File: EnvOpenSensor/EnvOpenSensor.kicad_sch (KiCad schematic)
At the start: 31 parts, among them J1 USB_C_Receptacle_USB2.0_16P, J2 AVR-ISP-6, SW1 SW_Push, SW2 SW_Push, SW3 SW_Push, SW4 SW_Push, U1 SCD41-D-R2, U2 Si7021-A20, U3 SPX3819M5-L-3-3, U4 ATtiny85-20S

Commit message: commit current version
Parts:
- added C0, C10, C11, C5: 0402 0.1uF, Capacitor_SMD:C_0402_1005Metric, symbol Device:C_Small
- added C12, C13, C6, C7: 0402 1uF, Capacitor_SMD:C_0402_1005Metric, symbol Device:C_Small
- added C14, C15, C8, C9: 0402 10uF, Capacitor_SMD:C_0402_1005Metric, symbol Device:C_Small
- added IC1, IC2, IC3, IC4: IS31FL3730-QFLS2-TR, Package_DFN_QFN:QFN-24-1EP_4x4mm_P0.5mm_EP2.6x2.6mm_ThermalVias, symbol IS31FL3730-QFLS2-TR:IS31FL3730-QFLS2-TR
- added NT0: NetTie_2, NetTie:NetTie-2_SMD_Pad0.5mm, symbol Device:NetTie_2
- H1, H2, H3, H4: value MountingHole -> DIY-305-ountingHole
- U3: value SPX3819M5-L-3-3 -> SPX3819DIY-305-5-L-3-3
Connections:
- net +3V3: now also IC1.3 (SDB), IC1.6 (AD), IC2.3 (SDB), IC3.3 (SDB), IC4.3 (SDB)
- net GND: now also C0.2, C10.2, C11.2, C12.2, C13.2, C14.2, C15.2, C5.2, C6.2, C7.2, C8.2, C9.2, IC1.20 (GND_1), IC1.25 (GND_2), IC2.20 (GND_1), IC2.25 (GND_2), IC3.20 (GND_1), IC3.25 (GND_2), IC4.20 (GND_1), IC4.25 (GND_2), IC4.6 (AD)
- net PB0: now also IC1.1 (SDA), IC2.1 (SDA), IC2.6 (AD), IC3.1 (SDA), IC4.1 (SDA)
- net PB2: now also IC1.2 (SCL), IC2.2 (SCL), IC3.2 (SCL), IC3.6 (AD), IC4.2 (SCL)
- net VBUS: now also NT0.1
- net IC2C2: now reaches DIY-305-0.1 (Col2)
- net IC2C2: now also DIY-305-1.12 (Row2), IC4.23 (C2)
- net IC2R6: now reaches DIY-305-0.10 (Row6)
- net IC2R6: now also IC4.13 (R6/C11)
- net IC2R5: now reaches DIY-305-0.11 (Row5)
- net IC2R5: now also DIY-305-1.13 (Col5), IC4.12 (R5)
- net IC2R2: now reaches DIY-305-0.12 (Row2)
- net IC2R2: now also DIY-305-1.1 (Col2), IC4.8 (R2)
- net IC2C5: now reaches DIY-305-0.13 (Col5)
- net IC2C5: now also DIY-305-1.11 (Row5), IC4.19 (C5)
- net IC2C4: now reaches DIY-305-0.14 (Col4)
- net IC2C4: now also DIY-305-1.4 (Row4), IC4.21 (C4)
- net IC2R1: now reaches DIY-305-0.2 (Row1)
- net IC2R1: now also DIY-305-1.5 (Col1), IC4.7 (R1)
- net IC2R3: now reaches DIY-305-0.3 (Row3)
- net IC2R3: now also DIY-305-1.8 (Col3), IC4.9 (R3)
- net IC2R4: now reaches DIY-305-0.4 (Row4)
- net IC2R4: now also DIY-305-1.14 (Col4), IC4.10 (R4)
- net IC2C1: now reaches DIY-305-0.5 (Col1)
- net IC2C1: now also DIY-305-1.2 (Row1), IC4.24 (C1)
- net IC2C8: now reaches DIY-305-0.7 (Dot)
- net IC2C8: now also IC4.16 (C8)
- net IC2C3: now reaches DIY-305-0.8 (Col3)
- net IC2C3: now also DIY-305-1.3 (Row3), IC4.22 (C3)
- net IC2R7: now reaches DIY-305-0.9 (Row7)
- net IC2R7: now also IC4.14 (R7/C10)
- net IC4R2: now reaches DIY-305-7.1 (Col2)
- net IC4R2: now also DIY-305-6.12 (Row2), IC3.8 (R2)
- net IC4C6: now reaches DIY-305-7.10 (Row6)
- net IC4C6: now also IC3.18 (C6)
- net IC4C5: now reaches DIY-305-7.11 (Row5)
- net IC4C5: now also DIY-305-6.13 (Col5), IC3.19 (C5)
- net IC4C2: now reaches DIY-305-7.12 (Row2)
- net IC4C2: now also DIY-305-6.1 (Col2), IC3.23 (C2)
- net IC4R5: now reaches DIY-305-7.13 (Col5)
- net IC4R5: now also DIY-305-6.11 (Row5), IC3.12 (R5)
- net IC4R4: now reaches DIY-305-7.14 (Col4)
- net IC4R4: now also DIY-305-6.4 (Row4), IC3.10 (R4)
- net IC4C1: now reaches DIY-305-7.2 (Row1)
- net IC4C1: now also DIY-305-6.5 (Col1), IC3.24 (C1)
- net IC4C3: now reaches DIY-305-7.3 (Row3)
- net IC4C3: now also DIY-305-6.8 (Col3), IC3.22 (C3)
- net IC4C4: now reaches DIY-305-7.4 (Row4)
- net IC4C4: now also DIY-305-6.14 (Col4), IC3.21 (C4)
- net IC4R1: now reaches DIY-305-7.5 (Col1)
- net IC4R1: now also DIY-305-6.2 (Row1), IC3.7 (R1)
- net IC4R8: now reaches DIY-305-7.7 (Dot)
- net IC4R8: now also IC3.15 (R8/C9)
- net IC4R3: now reaches DIY-305-7.8 (Col3)
- net IC4R3: now also DIY-305-6.3 (Row3), IC3.9 (R3)
- net IC4C7: now reaches DIY-305-7.9 (Row7)
- net IC4C7: now also IC3.17 (C7)
- net IC2C6: now reaches DIY-305-1.10 (Row6)
- net IC2C6: now also IC4.18 (C6)
- net IC2R8: now reaches DIY-305-1.7 (Dot)
- net IC2R8: now also IC4.15 (R8/C9)
- net IC2C7: now reaches DIY-305-1.9 (Row7)
- net IC2C7: now also IC4.17 (C7)
- net IC3R2: now reaches DIY-305-5.1 (Col2)
- net IC3R2: now also DIY-305-4.12 (Row2), IC2.8 (R2)
- net IC3C6: now reaches DIY-305-5.10 (Row6)
- net IC3C6: now also IC2.18 (C6)
- net IC3C5: now reaches DIY-305-5.11 (Row5)
- net IC3C5: now also DIY-305-4.13 (Col5), IC2.19 (C5)
- net IC3C2: now reaches DIY-305-5.12 (Row2)
- net IC3C2: now also DIY-305-4.1 (Col2), IC2.23 (C2)
- net IC3R5: now reaches DIY-305-5.13 (Col5)
- net IC3R5: now also DIY-305-4.11 (Row5), IC2.12 (R5)
- net IC3R4: now reaches DIY-305-5.14 (Col4)
- net IC3R4: now also DIY-305-4.4 (Row4), IC2.10 (R4)
- net IC3C1: now reaches DIY-305-5.2 (Row1)
- net IC3C1: now also DIY-305-4.5 (Col1), IC2.24 (C1)
- net IC3C3: now reaches DIY-305-5.3 (Row3)
- net IC3C3: now also DIY-305-4.8 (Col3), IC2.22 (C3)
- net IC3C4: now reaches DIY-305-5.4 (Row4)
- net IC3C4: now also DIY-305-4.14 (Col4), IC2.21 (C4)
- net IC3R1: now reaches DIY-305-5.5 (Col1)
- net IC3R1: now also DIY-305-4.2 (Row1), IC2.7 (R1)
- net IC3R8: now reaches DIY-305-5.7 (Dot)
- net IC3R8: now also IC2.15 (R8/C9)
- net IC3R3: now reaches DIY-305-5.8 (Col3)
- net IC3R3: now also DIY-305-4.3 (Row3), IC2.9 (R3)
- net IC3C7: now reaches DIY-305-5.9 (Row7)
- net IC3C7: now also IC2.17 (C7)
- net IC1R2: now reaches DIY-305-3.1 (Col2)
- net IC1R2: now also DIY-305-2.12 (Row2), IC1.8 (R2)
- net IC1C6: now reaches DIY-305-3.10 (Row6)
- net IC1C6: now also IC1.18 (C6)
- net IC1C5: now reaches DIY-305-3.11 (Row5)
- net IC1C5: now also DIY-305-2.13 (Col5), IC1.19 (C5)
- net IC1C2: now reaches DIY-305-3.12 (Row2)
- net IC1C2: now also DIY-305-2.1 (Col2), IC1.23 (C2)
- net IC1R5: now reaches DIY-305-3.13 (Col5)
- net IC1R5: now also DIY-305-2.11 (Row5), IC1.12 (R5)
- net IC1R4: now reaches DIY-305-3.14 (Col4)
- net IC1R4: now also DIY-305-2.4 (Row4), IC1.10 (R4)
- net IC1C1: now reaches DIY-305-3.2 (Row1)
- net IC1C1: now also DIY-305-2.5 (Col1), IC1.24 (C1)
- net IC1C3: now reaches DIY-305-3.3 (Row3)
- net IC1C3: now also DIY-305-2.8 (Col3), IC1.22 (C3)
- net IC1C4: now reaches DIY-305-3.4 (Row4)
- net IC1C4: now also DIY-305-2.14 (Col4), IC1.21 (C4)
- net IC1R1: now reaches DIY-305-3.5 (Col1)
- net IC1R1: now also DIY-305-2.2 (Row1), IC1.7 (R1)
- net IC1R8: now reaches DIY-305-3.7 (Dot)
- net IC1R8: now also IC1.15 (R8/C9)
- net IC1R3: now reaches DIY-305-3.8 (Col3)
- net IC1R3: now also DIY-305-2.3 (Row3), IC1.9 (R3)
- net IC1C7: now reaches DIY-305-3.9 (Row7)
- net IC1C7: now also IC1.17 (C7)
- net IC3R6: now reaches DIY-305-4.10 (Row6)
- net IC3R6: now also IC2.13 (R6/C11)
- net IC3C8: now reaches DIY-305-4.7 (Dot)
- net IC3C8: now also IC2.16 (C8)
- net IC3R7: now reaches DIY-305-4.9 (Row7)
- net IC3R7: now also IC2.14 (R7/C10)
- net IC1R6: now reaches DIY-305-2.10 (Row6)
- net IC1R6: now also IC1.13 (R6/C11)
- net IC1C8: now reaches DIY-305-2.7 (Dot)
- net IC1C8: now also IC1.16 (C8)
- net IC1R7: now reaches DIY-305-2.9 (Row7)
- net IC1R7: now also IC1.14 (R7/C10)
- net IC4R6: now reaches DIY-305-6.10 (Row6)
- net IC4R6: now also IC3.13 (R6/C11)
- net IC4C8: now reaches DIY-305-6.7 (Dot)
- net IC4C8: now also IC3.16 (C8)
- net IC4R7: now reaches DIY-305-6.9 (Row7)
- net IC4R7: now also IC3.14 (R7/C10)
- new net VCC: C0.1, C10.1, C11.1, C12.1, C13.1, C14.1, C15.1, C5.1, C6.1, C7.1, C8.1, C9.1, IC1.11 (VCC), IC2.11 (VCC), IC3.11 (VCC), IC4.11 (VCC), NT0.2

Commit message: let autorouter go crazy
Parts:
- added C16: 0402 0.1uF, Capacitor_SMD:C_0402_1005Metric, symbol Device:C_Small
- added C17: 0402 1uF, Capacitor_SMD:C_0402_1005Metric, symbol Device:C_Small
- added C18: 0402 10uF, Capacitor_SMD:C_0402_1005Metric, symbol Device:C_Small
- added R0, R10, R11, R12, R13, R14, R15, R16, R6, R7, R8, R9: 10K 0402, Resistor_SMD:R_0402_1005Metric, symbol Device:R_Small
- added U0: TCA9548ARGER, Package_DFN_QFN:Texas_RGE0024C_EP2.1x2.1mm, symbol Interface_Expansion:TCA9548ARGER
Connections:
- net +3V3: now also C16.1, C17.1, C18.1, R0.2, R10.2, R11.2, R12.2, R13.2, R14.2, R15.2, R16.2, R6.2, R7.2, R8.2, R9.2, U0.21 (VCC)
- net GND: now also C16.2, C17.2, C18.2, U0.18 (A2), U0.22 (A0), U0.23 (A1), U0.9 (GND)
- net PB0: now also U0.20 (SDA); no longer IC1.1 (SDA), IC2.1 (SDA), IC2.6 (AD), IC3.1 (SDA), IC4.1 (SDA), U1.10 (SDA), U2.1 (SDA)
- net PB2: now also U0.19 (SCL); no longer IC1.2 (SCL), IC2.2 (SCL), IC3.2 (SCL), IC3.6 (AD), IC4.2 (SCL), U1.9 (SCL), U2.6 (SCL)
- new net SCL0_3V3: R16.1, U0.2 (SC0), U2.6 (SCL)
- new net SCL1_3V3: R14.1, U0.4 (SC1), U1.9 (SCL)
- new net SCL2_3V3: IC1.2 (SCL), R7.1, U0.6 (SC2)
- new net SCL3_3V3: IC2.2 (SCL), R0.1, U0.8 (SC3)
- new net SCL4_3V3: IC3.2 (SCL), IC3.6 (AD), R9.1, U0.11 (SC4)
- new net SCL5_3V3: IC4.2 (SCL), R11.1, U0.13 (SC5)
- new net SCL6_3V3: U0.15 (SC6)
- new net SCL7_3V3: U0.17 (SC7)
- new net SDA0_3V3: R15.1, U0.1 (SD0), U2.1 (SDA)
- new net SDA1_3V3: R13.1, U0.3 (SD1), U1.10 (SDA)
- new net SDA2_3V3: IC1.1 (SDA), R8.1, U0.5 (SD2)
- new net SDA3_3V3: IC2.1 (SDA), IC2.6 (AD), R6.1, U0.7 (SD3)
- new net SDA4_3V3: IC3.1 (SDA), R10.1, U0.10 (SD4)
- new net SDA5_3V3: IC4.1 (SDA), R12.1, U0.12 (SD5)
- new net SDA6_3V3: U0.14 (SD6)
- new net SDA7_3V3: U0.16 (SD7)

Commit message: generated production files
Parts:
- J1: value USB_C_Receptacle_USB2.0_16P -> HRO_TYPE-C-31-M-12
- U3: value SPX3819DIY-305-5-L-3-3 -> LDO SOT-23-5 3.3V
- renumbered C1 to C_BYP_1
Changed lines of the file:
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@@
   (symbol (lib_id "Device:C_Small") (at 100.33 29.21 0) (unit 1)
     (in_bom yes) (on_board yes) (dnp no)
-    (property "Reference" "C1" (at 100.965 27.94 0)
+    (property "Reference" "C_BYP_1" (at 101.6 27.94 0)
       (effects (font (size 0.25 0.25)))
     )
@@
       (project "EnvOpenSensor"
         (path "/2bbc1dac-4f9d-46a0-a466-6585abe7fd58"
-          (reference "C1") (unit 1)
+          (reference "C_BYP_1") (unit 1)
         )
       )
@@
       (effects (font (size 1.27 1.27)))
     )
-    (property "Value" "SPX3819DIY-305-5-L-3-3" (at 92.075 17.78 0)
+    (property "Value" "LDO SOT-23-5 3.3V" (at 92.075 17.78 0)
       (effects (font (size 1.27 1.27)))
     )
@@
       (effects (font (size 1.27 1.27)))
     )
-    (property "Value" "USB_C_Receptacle_USB2.0_16P" (at 31.115 20.32 0)
-      (effects (font (size 1.27 1.27)))
-    )
+    (property "Value" "HRO_TYPE-C-31-M-12" (at 31.115 20.32 0)
+      (effects (font (size 1.27 1.27)))
+    )

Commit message: began re-work on fixing colossal mistakes
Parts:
- removed C10, C11, C5: 0402 0.1uF, Capacitor_SMD:C_0402_1005Metric, symbol Device:C_Small
- removed C12, C13, C7: 0402 1uF, Capacitor_SMD:C_0402_1005Metric, symbol Device:C_Small
- removed C14, C15, C9: 0402 10uF, Capacitor_SMD:C_0402_1005Metric, symbol Device:C_Small
- added C104, C107, C110: 0402 0.1uF, Capacitor_SMD:C_0402_1005Metric, symbol Device:C_Small
- added C105, C108, C111: 0402 1uF, Capacitor_SMD:C_0402_1005Metric, symbol Device:C_Small
- added C106, C109, C112: 0402 10uF, Capacitor_SMD:C_0402_1005Metric, symbol Device:C_Small
- renumbered C0 to C101, C6 to C102, C8 to C103, DIY-305-2 to DIY-305-1, DIY-305-3 to DIY-305-2, DIY-305-0 to DIY-305-3, DIY-305-1 to DIY-305-4, DIY-305-4 to DIY-305-5, DIY-305-5 to DIY-305-6, DIY-305-6 to DIY-305-7, DIY-305-7 to DIY-305-8, IC4 to IC2, IC2 to IC3, IC3 to IC4, R7 to R101, R8 to R102, R11 to R103, R12 to R104, R0 to R105, R6 to R106, R9 to R107, R10 to R108
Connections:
- net GND: now also C104.2, C105.2, C106.2, C107.2, C108.2, C109.2, C110.2, C111.2, C112.2
- net SCL2_3V3: no longer IC1.2 (SCL), R101.1
- net SCL3_3V3: no longer IC3.2 (SCL), R105.1
- net SCL5_3V3: now also IC3.2 (SCL), R105.1; no longer IC2.2 (SCL), R103.1
- net SCL6_3V3: now also IC2.2 (SCL), R103.1
- net SCL7_3V3: now also IC1.2 (SCL), R101.1
- net SDA2_3V3: no longer IC1.1 (SDA), R102.1
- net SDA3_3V3: no longer IC3.1 (SDA), IC3.6 (AD), R106.1
- net SDA5_3V3: now also IC3.1 (SDA), IC3.6 (AD), R106.1; no longer IC2.1 (SDA), R104.1
- net SDA6_3V3: now also IC2.1 (SDA), R104.1
- net SDA7_3V3: now also IC1.1 (SDA), R102.1
- net VCC: now also C104.1, C105.1, C106.1, C107.1, C108.1, C109.1, C110.1, C111.1, C112.1
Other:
- moved on the sheet: C101, C102, C103, DIY-305-1, DIY-305-2, DIY-305-3, DIY-305-4, DIY-305-5, DIY-305-6, DIY-305-7, DIY-305-8, IC1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

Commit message: swapped LDO for more capable switching regulator
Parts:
- removed C2, C3, C_BYP_1: 10nF 0402, Capacitor_SMD:C_0402_1005Metric, symbol Device:C_Small
- removed R3: 10K 0402, Resistor_SMD:R_0402_1005Metric, symbol Device:R_Small
- removed U3: LDO SOT-23-5 3.3V, Package_TO_SOT_SMD:SOT-23-5, symbol Regulator_Linear:SPX3819M5-L-3-3
- added C1, C6, C7: 10uF 0402, Capacitor_SMD:C_0402_1005Metric, symbol Device:C_Small
- added C5: 0.1uF 0402, Capacitor_SMD:C_0402_1005Metric, symbol Device:C_Small
- added L1: SPH3015H2R2MT, Inductor_SMD:L_Sunlord_SWPA3015S, symbol Device:L_Small
- added R6: 100ohm 0402, Resistor_SMD:R_0402_1005Metric, symbol Device:R_Small
- added U5: TPS63001DRCR, Package_SON:Texas_DRC0010J_ThermalVias, symbol Regulator_Switching:TPS63001
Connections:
- net +3V3: now also NT0.1, C6.1, C7.1, U5.1 (VOUT), U5.10 (FB)
- net GND: now also C1.2, C5.2, C6.2, C7.2, U5.11 (PGND), U5.3 (PGND), U5.9 (GND)
- net VBUS: now also C1.1, R6.1, U5.5 (VIN); no longer NT0.1
- new net: C5.1, R6.2, U5.6 (EN), U5.7 (PS/SYNC), U5.8 (VINA)
- new net: L1.2, U5.2 (L2)
- new net: L1.1, U5.4 (L1)
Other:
- moved on the sheet: C101, C102, C103, C104, C105, C106, C107, C108, C109, C110, C111, C112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

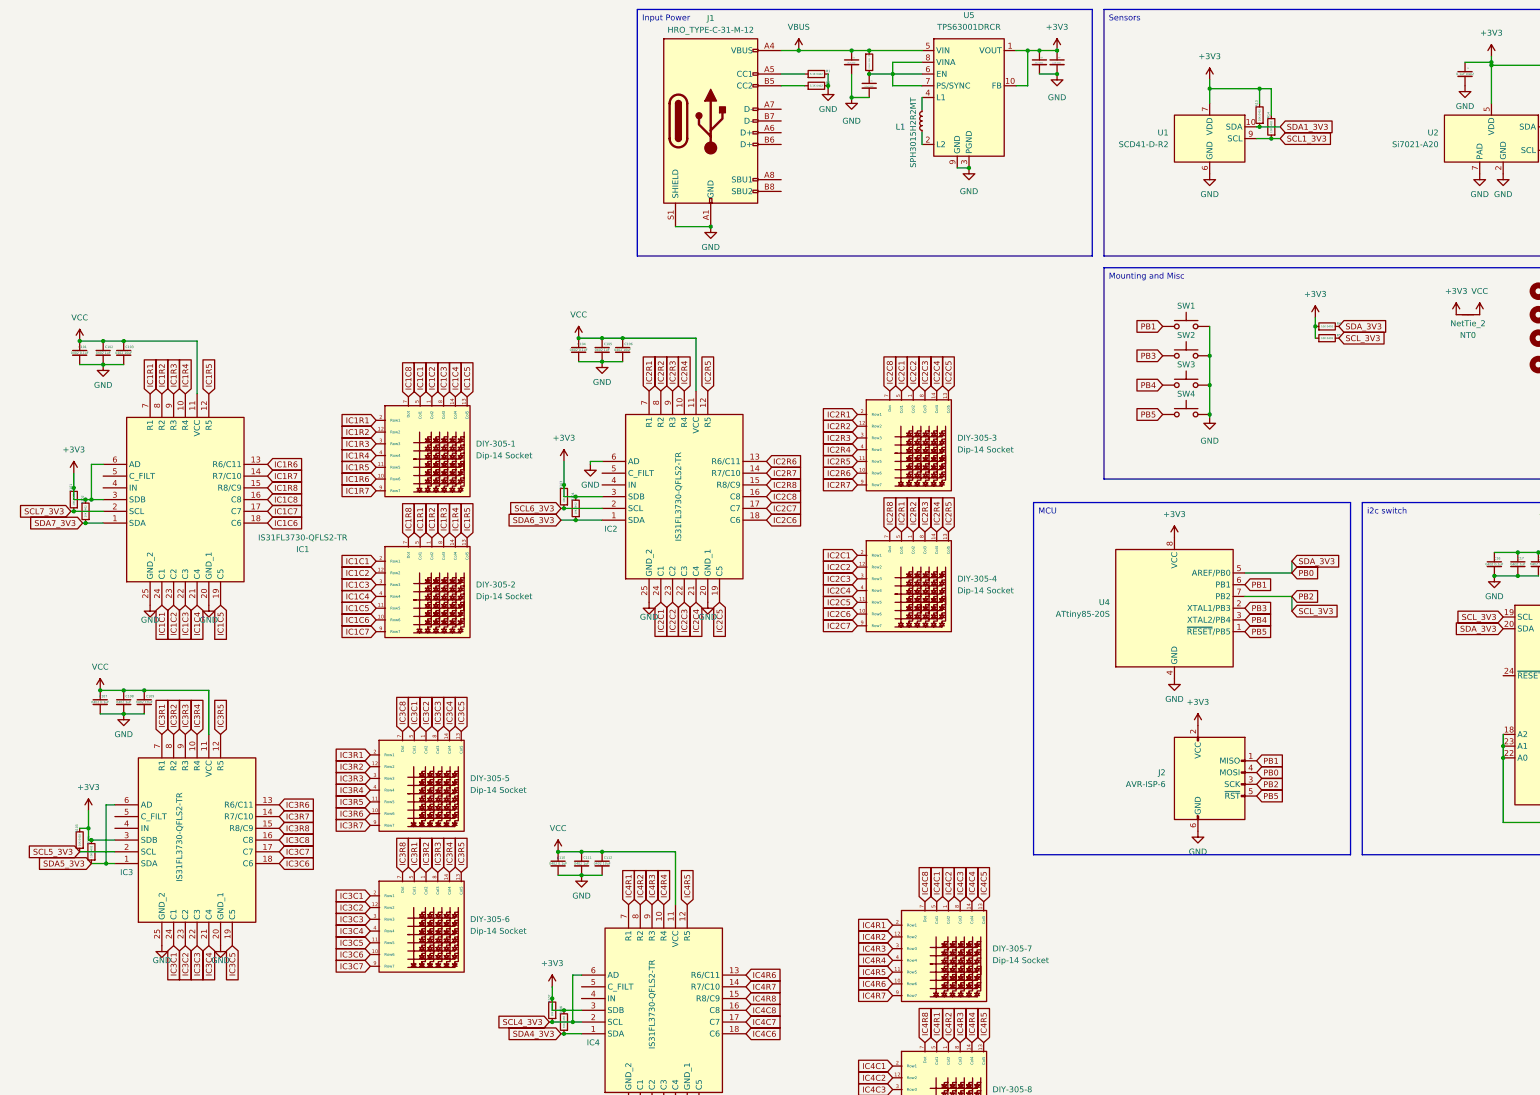
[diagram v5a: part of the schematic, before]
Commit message: re-drew all traces and moved some components about
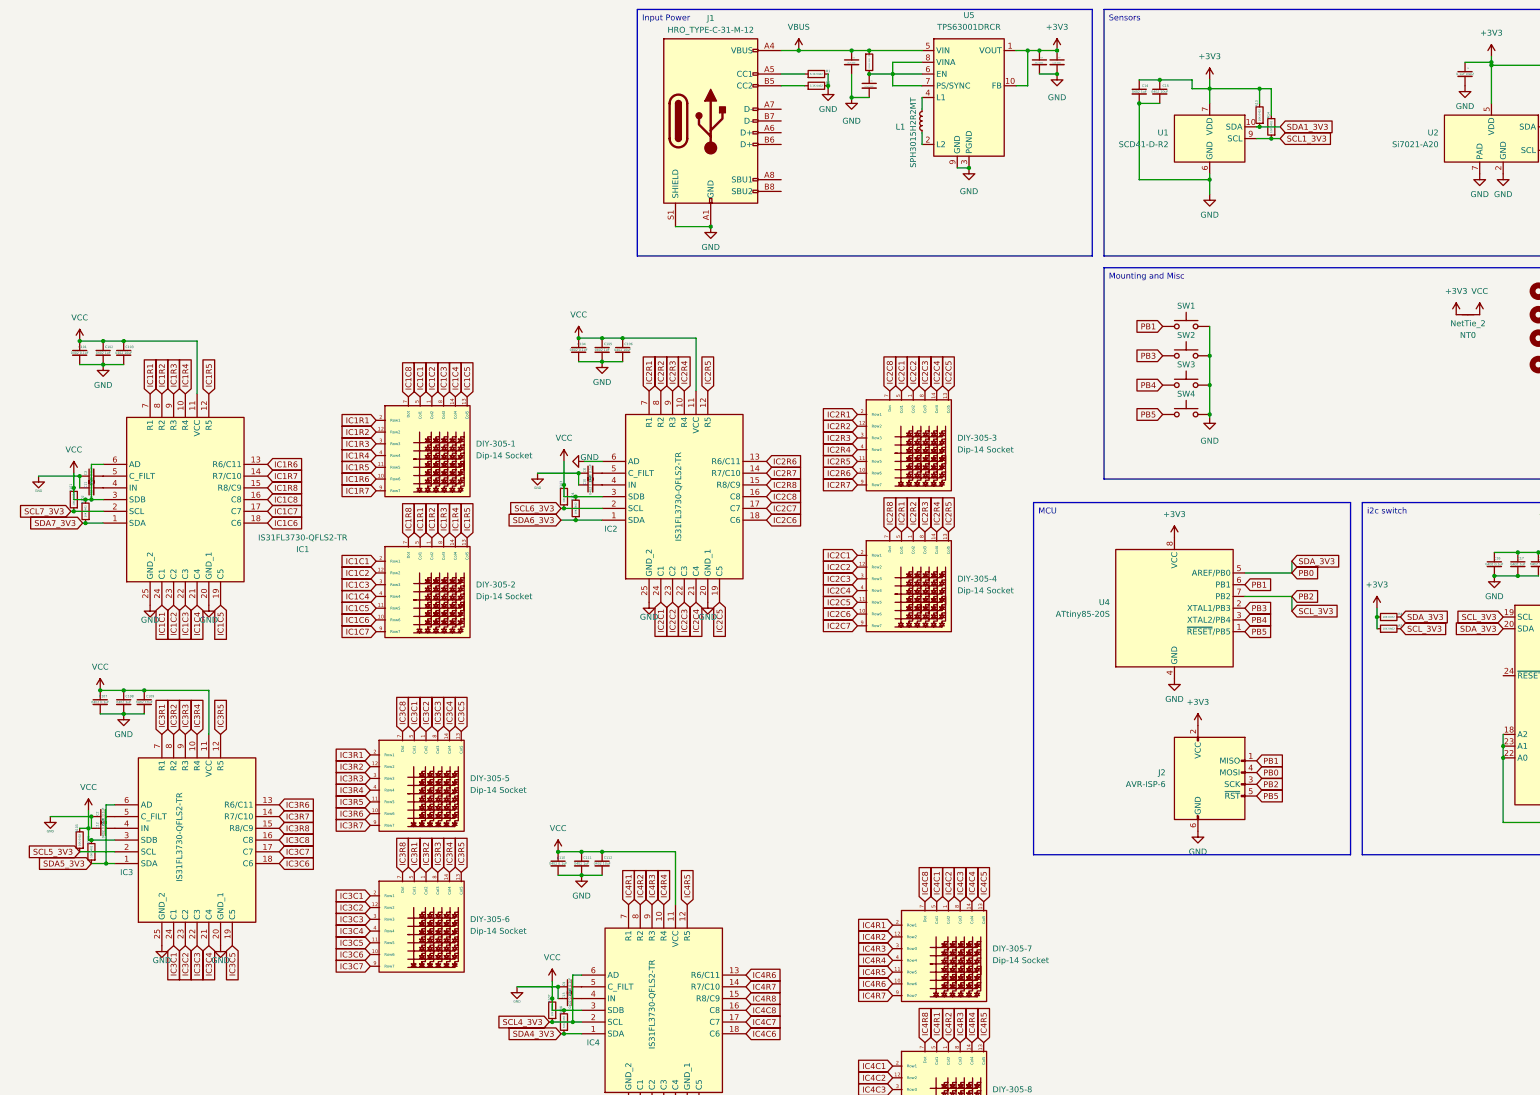
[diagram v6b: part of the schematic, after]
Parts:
- added C10, C11, C12, C13: 0402 0.22uF, Capacitor_SMD:C_0402_1005Metric, symbol Device:C_Small
- added C14: 0402 1uF, Capacitor_SMD:C_0402_1005Metric, symbol Device:C_Small
- added C15: 0402 10uF, Capacitor_SMD:C_0402_1005Metric, symbol Device:C_Small
- added C2, C3, C8, C9: 0402 0.1uF, Capacitor_SMD:C_0402_1005Metric, symbol Device:C_Small
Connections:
- net +3V3: now also C14.1, C15.1; no longer IC1.3 (SDB), IC1.6 (AD), IC2.3 (SDB), IC3.3 (SDB), IC4.3 (SDB), R101.2, R102.2, R103.2, R104.2, R105.2, R106.2, R107.2, R108.2
- net GND: now also C10.1, C11.1, C12.1, C13.1, C14.2, C15.2, C2.1, C3.1, C8.1, C9.1
- net VCC: now also IC1.3 (SDB), IC1.6 (AD), IC2.3 (SDB), IC3.3 (SDB), IC4.3 (SDB), R101.2, R102.2, R103.2, R104.2, R105.2, R106.2, R107.2, R108.2
- net at IC3.4 (IN): now also C12.2
- net at IC3.5 (C_FILT): now also C2.2
- net at IC1.4 (IN): now also C11.2
- net at IC1.5 (C_FILT): now also C3.2
- net at IC2.4 (IN): now also C10.2
- net at IC2.5 (C_FILT): now also C8.2
- net at IC4.4 (IN): now also C13.2
- net at IC4.5 (C_FILT): now also C9.2
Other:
- moved on the sheet: R4, R5
